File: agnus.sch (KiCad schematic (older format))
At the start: 34 parts, among them J101 Conn_01x03_Male, J102 Jumper_2_Open, J900 Jumper_2_Bridged, U101 AGNUS8372, U102 GARY5719, U107 74LS74A, U108 74LS74A, U302 74LS32, U900 74F00, X1 28.63636MHz

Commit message: Update footprints
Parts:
- C101, C102, C107, C108, C110, C905, C907, C908, C918: footprint (none) -> Capacitor_THT:C_Rect_L11.0mm_W2.8mm_P10.00mm_MKT
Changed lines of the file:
@@
 F 0 "C905" H 1615 1096 50  0000 L CNN
 F 1 "100pF" H 1615 1005 50  0000 L CNN
-F 2 "" H 1538 900 50  0001 C CNN
+F 2 "Capacitor_THT:C_Rect_L11.0mm_W2.8mm_P10.00mm_MKT" H 1538 900 50  0001 C CNN
 F 3 "~" H 1500 1050 50  0001 C CNN
 	1    1500 1050
@@
 F 0 "C110" H 3465 10546 50  0000 L CNN
 F 1 "0.1uF" H 3465 10455 50  0000 L CNN
-F 2 "" H 3388 10350 50  0001 C CNN
+F 2 "Capacitor_THT:C_Rect_L11.0mm_W2.8mm_P10.00mm_MKT" H 3388 10350 50  0001 C CNN
 F 3 "~" H 3350 10500 50  0001 C CNN
 	1    3350 10500
@@
 F 0 "C101" H 10765 4846 50  0000 L CNN
 F 1 "0.1uF" H 10765 4755 50  0000 L CNN
-F 2 "" H 10688 4650 50  0001 C CNN
+F 2 "Capacitor_THT:C_Rect_L11.0mm_W2.8mm_P10.00mm_MKT" H 10688 4650 50  0001 C CNN
 F 3 "~" H 10650 4800 50  0001 C CNN
 	1    10650 4800
@@
 F 0 "C102" H 2415 10546 50  0000 L CNN
 F 1 "0.1uF" H 2415 10455 50  0000 L CNN
-F 2 "" H 2338 10350 50  0001 C CNN
+F 2 "Capacitor_THT:C_Rect_L11.0mm_W2.8mm_P10.00mm_MKT" H 2338 10350 50  0001 C CNN
 F 3 "~" H 2300 10500 50  0001 C CNN
 	1    2300 10500
@@
 F 0 "C907" H 4115 4546 50  0000 L CNN
 F 1 "100pF" H 4115 4455 50  0000 L CNN
-F 2 "" H 4038 4350 50  0001 C CNN
+F 2 "Capacitor_THT:C_Rect_L11.0mm_W2.8mm_P10.00mm_MKT" H 4038 4350 50  0001 C CNN
 F 3 "~" H 4000 4500 50  0001 C CNN
 	1    4000 4500
@@
 F 0 "C908" H 4615 4546 50  0000 L CNN
 F 1 "100pF" H 4615 4455 50  0000 L CNN
-F 2 "" H 4538 4350 50  0001 C CNN
+F 2 "Capacitor_THT:C_Rect_L11.0mm_W2.8mm_P10.00mm_MKT" H 4538 4350 50  0001 C CNN
 F 3 "~" H 4500 4500 50  0001 C CNN
 	1    4500 4500
@@
 F 0 "C918" H 13065 7096 50  0000 L CNN
 F 1 "0.1uF" H 13065 7005 50  0000 L CNN
-F 2 "" H 12988 6900 50  0001 C CNN
+F 2 "Capacitor_THT:C_Rect_L11.0mm_W2.8mm_P10.00mm_MKT" H 12988 6900 50  0001 C CNN
 F 3 "~" H 12950 7050 50  0001 C CNN
 	1    12950 7050
@@
 F 0 "C108" H 14315 7046 50  0000 L CNN
 F 1 "0.1uF" H 14315 6955 50  0000 L CNN
-F 2 "" H 14238 6850 50  0001 C CNN
+F 2 "Capacitor_THT:C_Rect_L11.0mm_W2.8mm_P10.00mm_MKT" H 14238 6850 50  0001 C CNN
 F 3 "~" H 14200 7000 50  0001 C CNN
 	1    14200 7000
@@
 F 0 "C107" H 15565 7046 50  0000 L CNN
 F 1 "0.1uF" H 15565 6955 50  0000 L CNN
-F 2 "" H 15488 6850 50  0001 C CNN
+F 2 "Capacitor_THT:C_Rect_L11.0mm_W2.8mm_P10.00mm_MKT" H 15488 6850 50  0001 C CNN
 F 3 "~" H 15450 7000 50  0001 C CNN
 	1    15450 7000

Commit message: More placement
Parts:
- J101: footprint Connector_PinSocket_2.54mm:PinSocket_1x03_P2.54mm_Vertical -> Connector_PinHeader_2.54mm:PinHeader_1x03_P2.54mm_Vertical
- J900: footprint Connector_PinSocket_2.54mm:PinSocket_2x01_P2.54mm_Vertical -> Connector_PinHeader_2.54mm:PinHeader_2x01_P2.54mm_Vertical
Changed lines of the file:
@@
 F 0 "J900" H 1400 3100 50  0000 C CNN
 F 1 "Jumper_2_Bridged" H 1400 3304 50  0001 C CNN
-F 2 "Connector_PinSocket_2.54mm:PinSocket_2x01_P2.54mm_Vertical" H 1400 3200 50  0001 C CNN
+F 2 "Connector_PinHeader_2.54mm:PinHeader_2x01_P2.54mm_Vertical" H 1400 3200 50  0001 C CNN
 F 3 "~" H 1400 3200 50  0001 C CNN
 	1    1400 3200
@@
 F 0 "J101" H 6508 6539 50  0000 C CNN
 F 1 "Conn_01x03_Male" H 6508 6540 50  0001 C CNN
-F 2 "Connector_PinSocket_2.54mm:PinSocket_1x03_P2.54mm_Vertical" H 6400 6350 50  0001 C CNN
+F 2 "Connector_PinHeader_2.54mm:PinHeader_1x03_P2.54mm_Vertical" H 6400 6350 50  0001 C CNN
 F 3 "~" H 6400 6350 50  0001 C CNN
 	1    6400 6350

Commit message: Make caps footprint smaller
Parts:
- C101, C102, C107, C108, C110, C905, C907, C908, C918: footprint Capacitor_THT:C_Rect_L11.0mm_W2.8mm_P10.00mm_MKT -> Capacitor_THT:C_Rect_L11.5mm_W2.0mm_P10.00mm_MKT
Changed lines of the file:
@@
 F 0 "C905" H 1615 1096 50  0000 L CNN
 F 1 "100pF" H 1615 1005 50  0000 L CNN
-F 2 "Capacitor_THT:C_Rect_L11.0mm_W2.8mm_P10.00mm_MKT" H 1538 900 50  0001 C CNN
+F 2 "Capacitor_THT:C_Rect_L11.5mm_W2.0mm_P10.00mm_MKT" H 1538 900 50  0001 C CNN
 F 3 "~" H 1500 1050 50  0001 C CNN
 	1    1500 1050
@@
 F 0 "C110" H 3465 10546 50  0000 L CNN
 F 1 "0.1uF" H 3465 10455 50  0000 L CNN
-F 2 "Capacitor_THT:C_Rect_L11.0mm_W2.8mm_P10.00mm_MKT" H 3388 10350 50  0001 C CNN
+F 2 "Capacitor_THT:C_Rect_L11.5mm_W2.0mm_P10.00mm_MKT" H 3388 10350 50  0001 C CNN
 F 3 "~" H 3350 10500 50  0001 C CNN
 	1    3350 10500
@@
 F 0 "C101" H 10765 4846 50  0000 L CNN
 F 1 "0.1uF" H 10765 4755 50  0000 L CNN
-F 2 "Capacitor_THT:C_Rect_L11.0mm_W2.8mm_P10.00mm_MKT" H 10688 4650 50  0001 C CNN
+F 2 "Capacitor_THT:C_Rect_L11.5mm_W2.0mm_P10.00mm_MKT" H 10688 4650 50  0001 C CNN
 F 3 "~" H 10650 4800 50  0001 C CNN
 	1    10650 4800
@@
 F 0 "C102" H 2415 10546 50  0000 L CNN
 F 1 "0.1uF" H 2415 10455 50  0000 L CNN
-F 2 "Capacitor_THT:C_Rect_L11.0mm_W2.8mm_P10.00mm_MKT" H 2338 10350 50  0001 C CNN
+F 2 "Capacitor_THT:C_Rect_L11.5mm_W2.0mm_P10.00mm_MKT" H 2338 10350 50  0001 C CNN
 F 3 "~" H 2300 10500 50  0001 C CNN
 	1    2300 10500
@@
 F 0 "C907" H 4115 4546 50  0000 L CNN
 F 1 "100pF" H 4115 4455 50  0000 L CNN
-F 2 "Capacitor_THT:C_Rect_L11.0mm_W2.8mm_P10.00mm_MKT" H 4038 4350 50  0001 C CNN
+F 2 "Capacitor_THT:C_Rect_L11.5mm_W2.0mm_P10.00mm_MKT" H 4038 4350 50  0001 C CNN
 F 3 "~" H 4000 4500 50  0001 C CNN
 	1    4000 4500
@@
 F 0 "C908" H 4615 4546 50  0000 L CNN
 F 1 "100pF" H 4615 4455 50  0000 L CNN
-F 2 "Capacitor_THT:C_Rect_L11.0mm_W2.8mm_P10.00mm_MKT" H 4538 4350 50  0001 C CNN
+F 2 "Capacitor_THT:C_Rect_L11.5mm_W2.0mm_P10.00mm_MKT" H 4538 4350 50  0001 C CNN
 F 3 "~" H 4500 4500 50  0001 C CNN
 	1    4500 4500
@@
 F 0 "C918" H 13065 7096 50  0000 L CNN
 F 1 "0.1uF" H 13065 7005 50  0000 L CNN
-F 2 "Capacitor_THT:C_Rect_L11.0mm_W2.8mm_P10.00mm_MKT" H 12988 6900 50  0001 C CNN
+F 2 "Capacitor_THT:C_Rect_L11.5mm_W2.0mm_P10.00mm_MKT" H 12988 6900 50  0001 C CNN
 F 3 "~" H 12950 7050 50  0001 C CNN
 	1    12950 7050
@@
 F 0 "C108" H 14315 7046 50  0000 L CNN
 F 1 "0.1uF" H 14315 6955 50  0000 L CNN
-F 2 "Capacitor_THT:C_Rect_L11.0mm_W2.8mm_P10.00mm_MKT" H 14238 6850 50  0001 C CNN
+F 2 "Capacitor_THT:C_Rect_L11.5mm_W2.0mm_P10.00mm_MKT" H 14238 6850 50  0001 C CNN
 F 3 "~" H 14200 7000 50  0001 C CNN
 	1    14200 7000
@@
 F 0 "C107" H 15565 7046 50  0000 L CNN
 F 1 "0.1uF" H 15565 6955 50  0000 L CNN
-F 2 "Capacitor_THT:C_Rect_L11.0mm_W2.8mm_P10.00mm_MKT" H 15488 6850 50  0001 C CNN
+F 2 "Capacitor_THT:C_Rect_L11.5mm_W2.0mm_P10.00mm_MKT" H 15488 6850 50  0001 C CNN
 F 3 "~" H 15450 7000 50  0001 C CNN
 	1    15450 7000

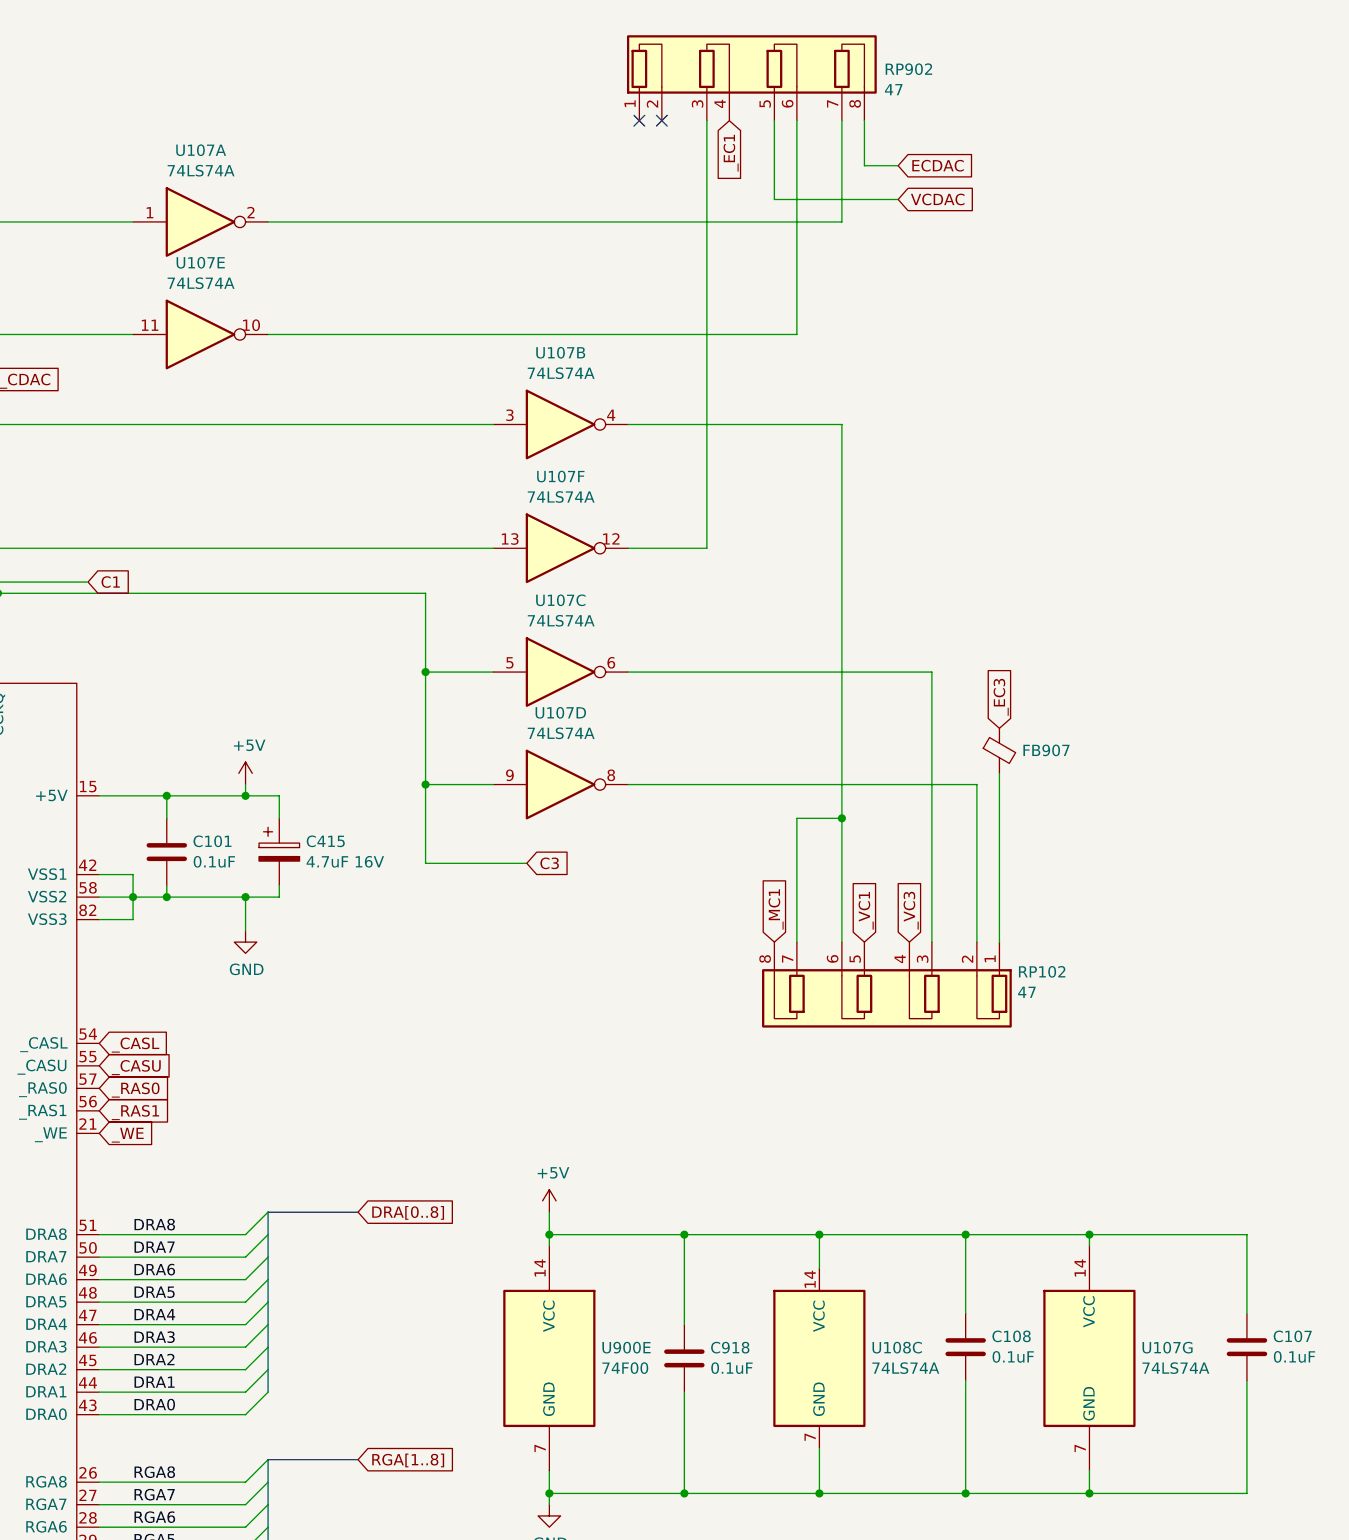
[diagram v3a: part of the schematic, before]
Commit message: Correct some datasheets
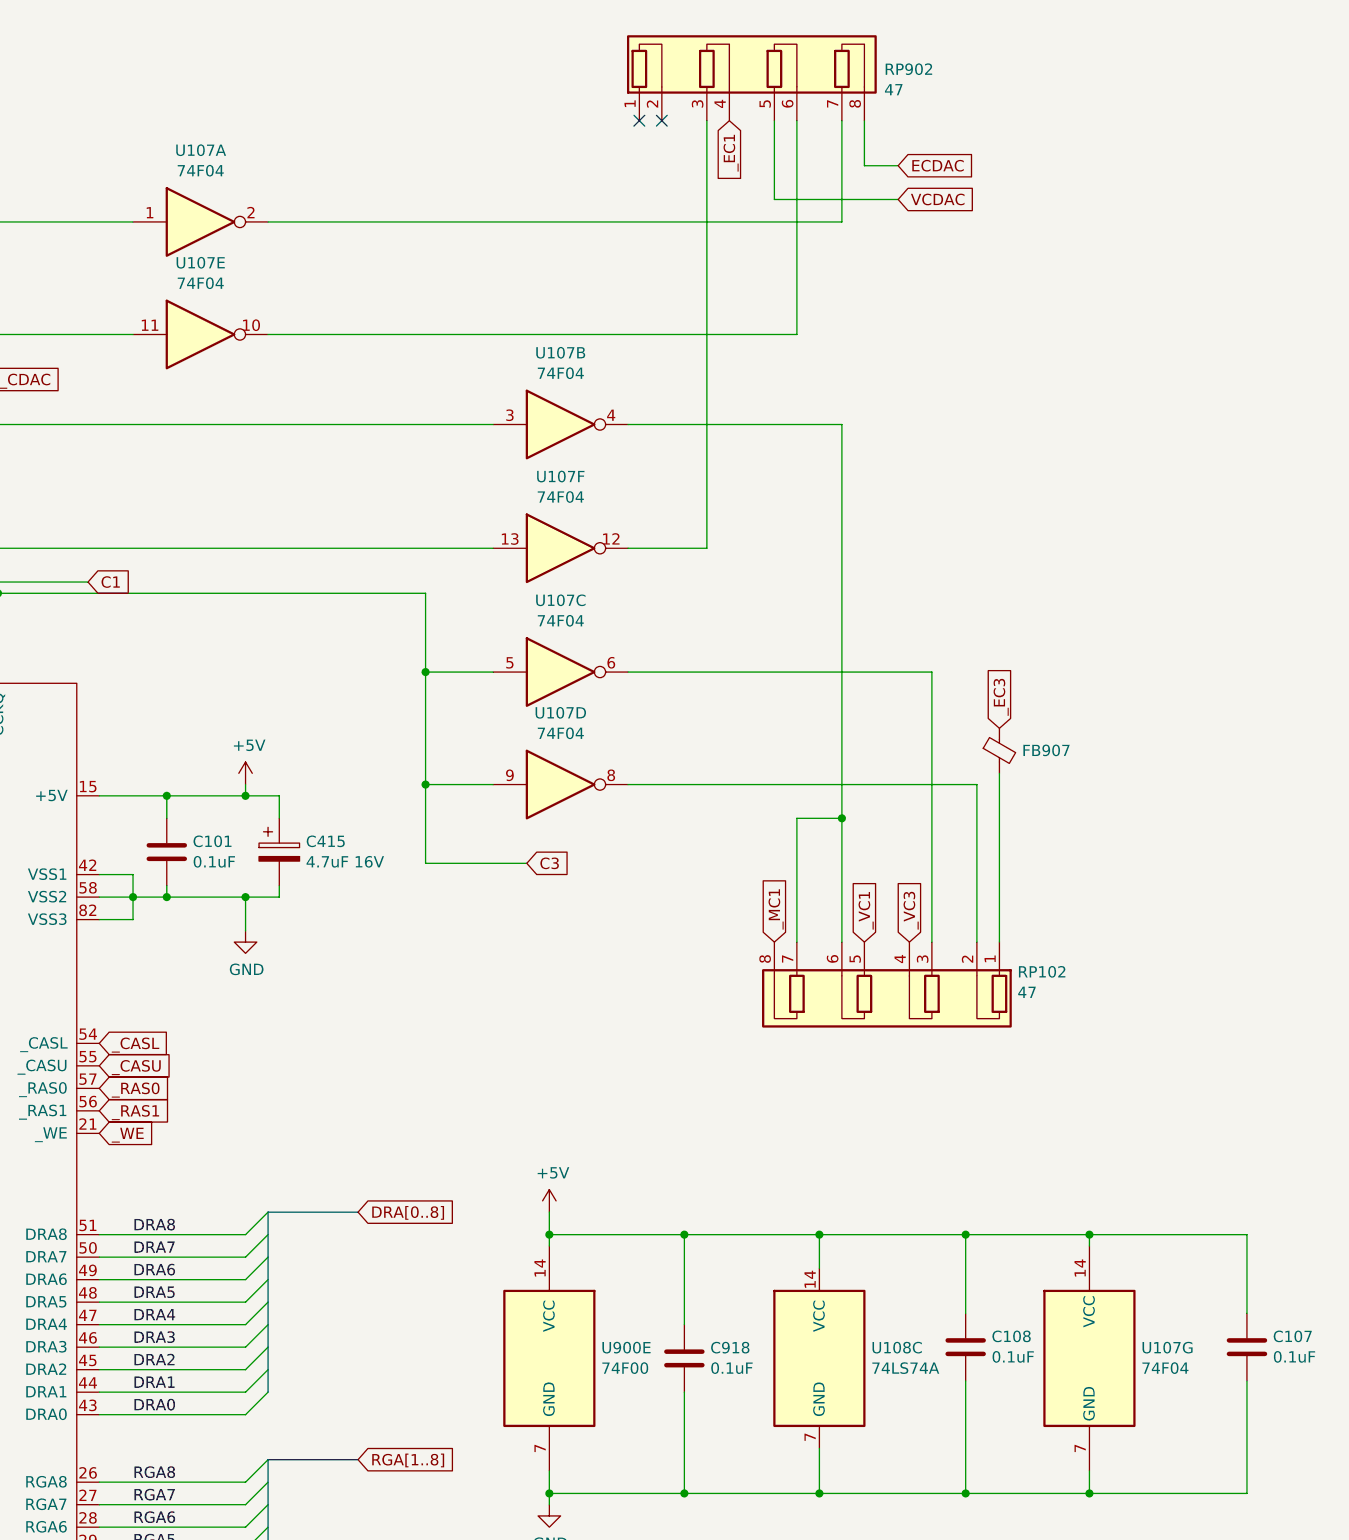
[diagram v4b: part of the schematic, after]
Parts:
- U107: value 74LS74A -> 74F04
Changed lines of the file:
@@
 F 1 "74F00" H 5050 3334 50  0000 C CNN
 F 2 "Package_DIP:DIP-14_W7.62mm_Socket" H 5050 3100 50  0001 C CNN
-F 3 "http://www.ti.com/lit/gpn/sn74ls00" H 5050 3100 50  0001 C CNN
+F 3 "http://www.ti.com/lit/ds/symlink/sn74f00.pdf" H 5050 3100 50  0001 C CNN
 	3    5050 3100
 	-1   0    0    -1
@@
 F 1 "74F00" H 5950 2974 50  0000 C CNN
 F 2 "Package_DIP:DIP-14_W7.62mm_Socket" H 5950 3200 50  0001 C CNN
-F 3 "http://www.ti.com/lit/gpn/sn74ls00" H 5950 3200 50  0001 C CNN
+F 3 "http://www.ti.com/lit/ds/symlink/sn74f00.pdf" H 5950 3200 50  0001 C CNN
 	4    5950 3200
 	-1   0    0    1
@@
 F 1 "28.63636MHz" H 4600 10800 50  0000 R CNN
 F 2 "Oscillator:Oscillator_DIP-14" H 4450 10150 50  0001 C CNN
-F 3 "http://www.conwin.com/datasheets/cx/cx030.pdf" H 3900 10500 50  0001 C CNN
+F 3 "" H 3900 10500 50  0001 C CNN
 	1    4000 10500
 	1    0    0    -1
@@
 P 10800 2000
 F 0 "U107" H 10800 2317 50  0000 C CNN
-F 1 "74LS74A" H 10800 2226 50  0000 C CNN
+F 1 "74F04" H 10800 2226 50  0000 C CNN
 F 2 "Package_DIP:DIP-14_W7.62mm_Socket" H 10800 2000 50  0001 C CNN
-F 3 "74xx/74hc_hct74.pdf" H 10800 2000 50  0001 C CNN
+F 3 "https://www.soemtron.org/downloads/disposals/74f04.pdf" H 10800 2000 50  0001 C CNN
 	1    10800 2000
 	1    0    0    -1
@@
 P 10800 2500
 F 0 "U107" H 10800 2817 50  0000 C CNN
-F 1 "74LS74A" H 10800 2726 50  0000 C CNN
+F 1 "74F04" H 10800 2726 50  0000 C CNN
 F 2 "Package_DIP:DIP-14_W7.62mm_Socket" H 10800 2500 50  0001 C CNN
-F 3 "74xx/74hc_hct74.pdf" H 10800 2500 50  0001 C CNN
+F 3 "https://www.soemtron.org/downloads/disposals/74f04.pdf" H 10800 2500 50  0001 C CNN
 	5    10800 2500
 	1    0    0    -1
@@
 P 12400 2900
 F 0 "U107" H 12400 3217 50  0000 C CNN
-F 1 "74LS74A" H 12400 3126 50  0000 C CNN
+F 1 "74F04" H 12400 3126 50  0000 C CNN
 F 2 "Package_DIP:DIP-14_W7.62mm_Socket" H 12400 2900 50  0001 C CNN
-F 3 "74xx/74hc_hct74.pdf" H 12400 2900 50  0001 C CNN
+F 3 "https://www.soemtron.org/downloads/disposals/74f04.pdf" H 12400 2900 50  0001 C CNN
 	2    12400 2900
 	1    0    0    -1
@@
 P 12400 3450
 F 0 "U107" H 12400 3767 50  0000 C CNN
-F 1 "74LS74A" H 12400 3676 50  0000 C CNN
+F 1 "74F04" H 12400 3676 50  0000 C CNN
 F 2 "Package_DIP:DIP-14_W7.62mm_Socket" H 12400 3450 50  0001 C CNN
-F 3 "74xx/74hc_hct74.pdf" H 12400 3450 50  0001 C CNN
+F 3 "https://www.soemtron.org/downloads/disposals/74f04.pdf" H 12400 3450 50  0001 C CNN
 	6    12400 3450
 	1    0    0    -1
@@
 P 12400 4000
 F 0 "U107" H 12400 4317 50  0000 C CNN
-F 1 "74LS74A" H 12400 4226 50  0000 C CNN
+F 1 "74F04" H 12400 4226 50  0000 C CNN
 F 2 "Package_DIP:DIP-14_W7.62mm_Socket" H 12400 4000 50  0001 C CNN
-F 3 "74xx/74hc_hct74.pdf" H 12400 4000 50  0001 C CNN
+F 3 "https://www.soemtron.org/downloads/disposals/74f04.pdf" H 12400 4000 50  0001 C CNN
 	3    12400 4000
 	1    0    0    -1
@@
 P 12400 4500
 F 0 "U107" H 12400 4817 50  0000 C CNN
-F 1 "74LS74A" H 12400 4726 50  0000 C CNN
+F 1 "74F04" H 12400 4726 50  0000 C CNN
 F 2 "Package_DIP:DIP-14_W7.62mm_Socket" H 12400 4500 50  0001 C CNN
-F 3 "74xx/74hc_hct74.pdf" H 12400 4500 50  0001 C CNN
+F 3 "https://www.soemtron.org/downloads/disposals/74f04.pdf" H 12400 4500 50  0001 C CNN
 	4    12400 4500
 	1    0    0    -1
@@
 F 1 "74F00" H 12120 7005 50  0000 R CNN
 F 2 "Package_DIP:DIP-14_W7.62mm_Socket" H 12350 7050 50  0001 C CNN
-F 3 "http://www.ti.com/lit/gpn/sn74ls00" H 12350 7050 50  0001 C CNN
+F 3 "http://www.ti.com/lit/ds/symlink/sn74f00.pdf" H 12350 7050 50  0001 C CNN
 	5    12350 7050
 	-1   0    0    -1
@@
 F 1 "74LS74A" H 13780 7005 50  0000 L CNN
 F 2 "Package_DIP:DIP-14_W7.62mm_Socket" H 13550 7050 50  0001 C CNN
-F 3 "74xx/74hc_hct74.pdf" H 13550 7050 50  0001 C CNN
+F 3 "http://www.ti.com/lit/ds/symlink/sn74ls74a.pdf" H 13550 7050 50  0001 C CNN
 	3    13550 7050
 	1    0    0    -1
@@
 P 14750 7050
 F 0 "U107" H 14980 7096 50  0000 L CNN
-F 1 "74LS74A" H 14980 7005 50  0000 L CNN
+F 1 "74F04" H 14980 7005 50  0000 L CNN
 F 2 "Package_DIP:DIP-14_W7.62mm_Socket" H 14750 7050 50  0001 C CNN
-F 3 "74xx/74hc_hct74.pdf" H 14750 7050 50  0001 C CNN
+F 3 "https://www.soemtron.org/downloads/disposals/74f04.pdf" H 14750 7050 50  0001 C CNN
 	7    14750 7050
 	1    0    0    -1
